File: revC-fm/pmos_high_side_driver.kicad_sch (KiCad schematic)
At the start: 4 parts, among them Q34 MMDT3946

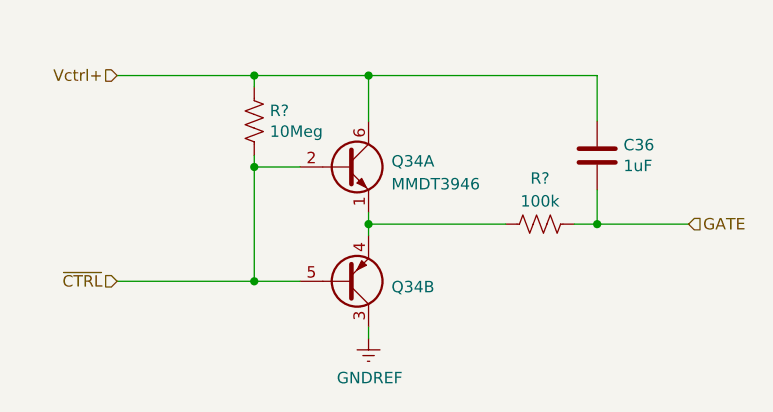
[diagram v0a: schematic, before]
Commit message: updated analog , solar comp, layout
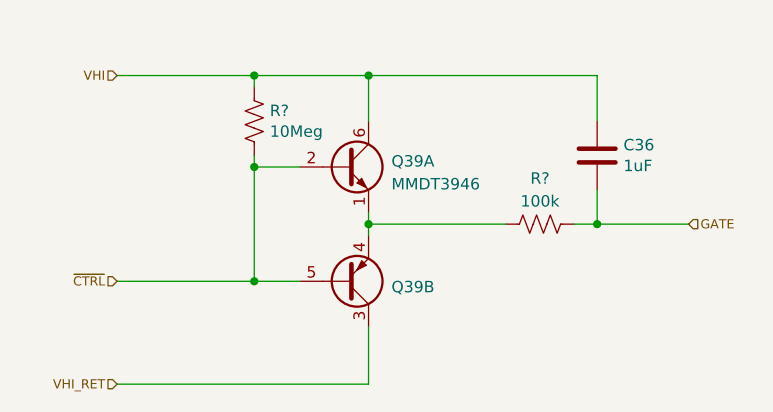
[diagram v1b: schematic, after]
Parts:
- renumbered Q34 to Q39
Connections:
- net GNDREF renamed VHI_RET
- net Vctrl+ renamed VHI

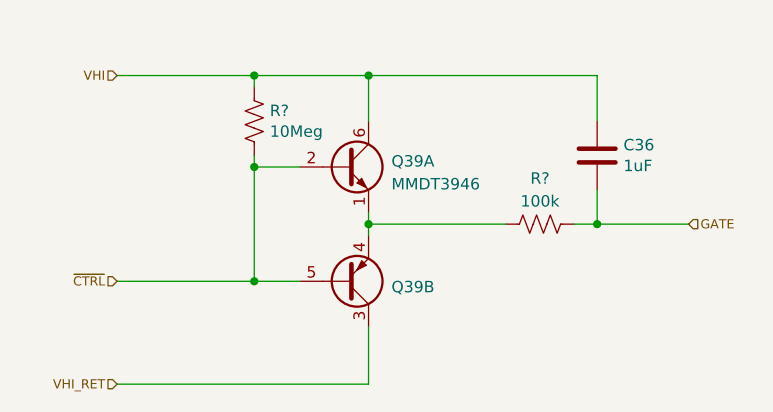
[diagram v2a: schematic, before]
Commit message: changed RF connector to TH
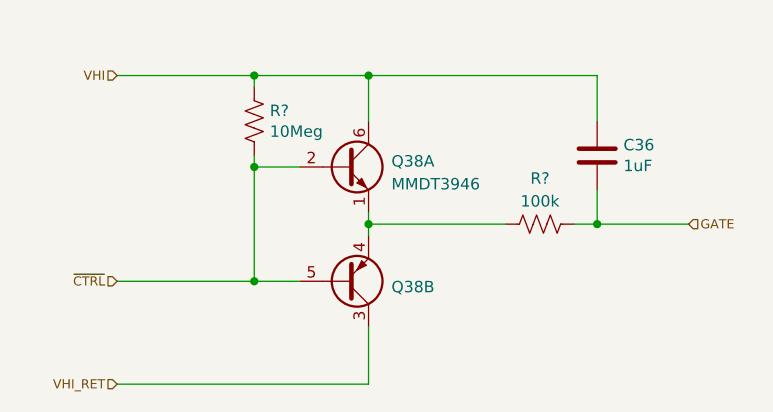
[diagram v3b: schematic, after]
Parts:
- renumbered Q39 to Q38

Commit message: working revC review changes
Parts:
- renumbered Q38 to Q40

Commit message: working revC
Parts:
- removed R?: 10Meg, Resistor_SMD:R_0603_1608Metric, symbol Device:R_US
- added R98: 0, Resistor_SMD:R_0603_1608Metric, symbol Device:R_US
- added R?: 10Meg, Resistor_SMD:R_0402_1005Metric, symbol Device:R_US
- C36: value 1uF -> 0.1uF; footprint Capacitor_SMD:C_0603_1608Metric -> Capacitor_SMD:C_0402_1005Metric
- Q27: renamed from Q40; Mfr. Part No (none) -> MMDT3946-7-F
- R?: footprint Resistor_SMD:R_0603_1608Metric -> Resistor_SMD:R_0402_1005Metric
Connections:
- net VHI: now also R98.1; no longer C36.1, Q27.6 (C1)
- net ~{CTRL}: now also R?.2
- new net: C36.1, Q27.6 (C1), R98.2, R?.1
